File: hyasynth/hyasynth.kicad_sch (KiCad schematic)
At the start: 43 parts, among them J1 Conn_01x04_Male, J2 Conn_01x03_Male, J3 Conn_01x09_Male, J4 Conn_01x05_Male, SW1 Power Switch, SW10 G# Ab, SW11 A, SW12 A# Bb, SW13 B, SW14 C, SW15 Down Octave, SW16 Function, SW17 Up Octave, SW18 Reset, SW2 Low C, SW3 C# Db, SW4 D, SW5 D# Eb, SW6 E, SW7 F, SW8 F# Gb, SW9 G, U1 EFM8LB12F64E-B-QFN32, U2 BH3544F, U3 PAM8302AAD

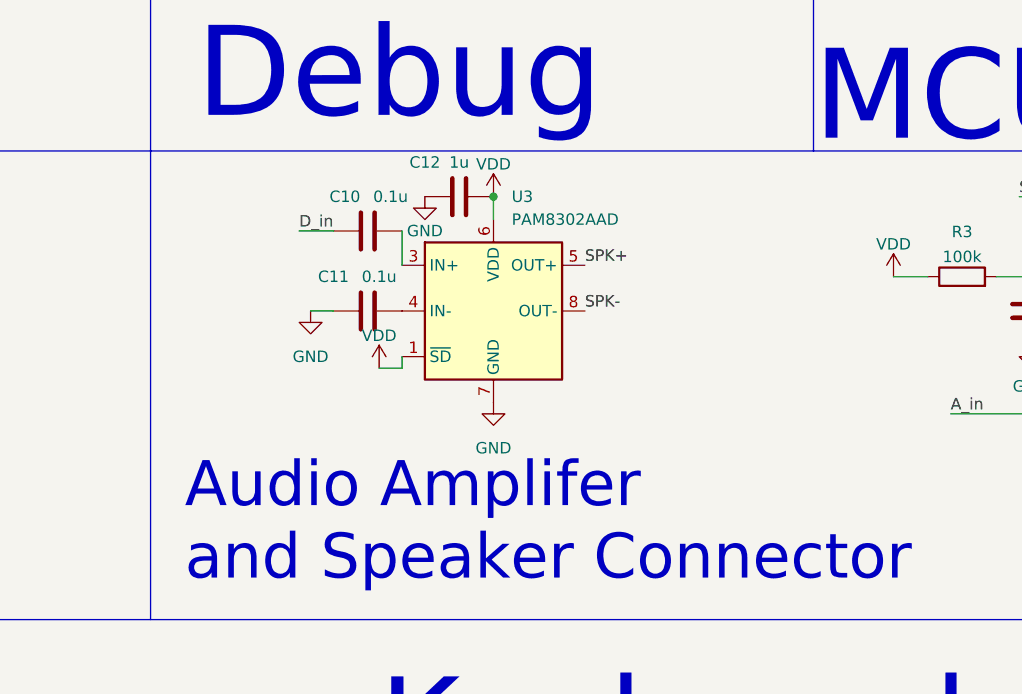
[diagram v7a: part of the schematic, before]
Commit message: started laying out pcb
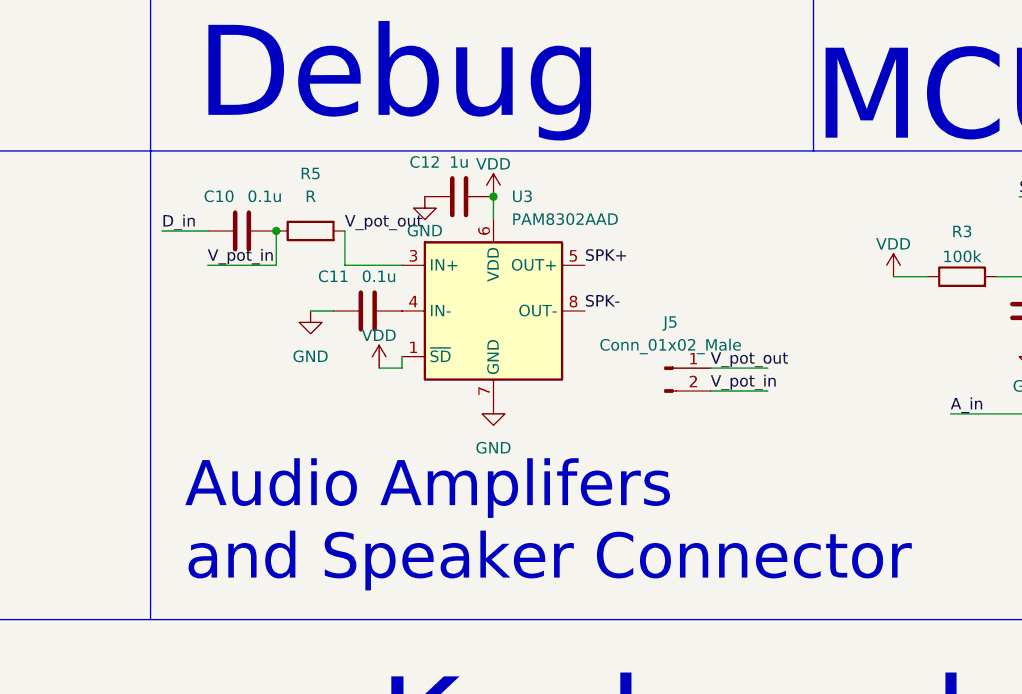
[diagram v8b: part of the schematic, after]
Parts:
- added J5: Conn_01x02_Male, Connector_PinHeader_2.54mm:PinHeader_1x02_P2.54mm_Vertical, symbol Connector:Conn_01x02_Male
- added R5: R, Resistor_SMD:R_0805_2012Metric_Pad1.20x1.40mm_HandSolder, symbol Device:R
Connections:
- net V_pot_in: now reaches C10.2
- net V_pot_in: now also J5.2 (Pin_2), R5.1; no longer U3.3 (IN+)
- new net V_pot_out: J5.1 (Pin_1), R5.2, U3.3 (IN+)
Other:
- note added: "Audio Amplifers and Speaker Connector"
- note removed: "Audio Amplifer and Speaker Connector"
- moved on the sheet: C10
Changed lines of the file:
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@@
   (junction (at 238.76 97.79) (diameter 0) (color 0 0 0 0)
+  )
+  (junction (at 91.44 92.71) (diameter 0) (color 0 0 0 0)
   )
   (junction (at 21.59 175.26) (diameter 0) (color 0 0 0 0)
@@
     (stroke (width 0) (type default) (color 0 0 0 0))
   )
+  (wire (pts (xy 99.06 96.52) (xy 105.41 96.52))
+    (stroke (width 0) (type default) (color 0 0 0 0))
+  )
   (wire (pts (xy 97.79 34.29) (xy 100.33 34.29))
     (stroke (width 0) (type default) (color 0 0 0 0))
@@
     (stroke (width 0) (type default) (color 0 0 0 0))
   )
-  (wire (pts (xy 105.41 92.71) (xy 105.41 96.52))
-    (stroke (width 0) (type default) (color 0 0 0 0))
-  )
-  (wire (pts (xy 93.98 92.71) (xy 97.79 92.71))
+  (wire (pts (xy 78.74 92.71) (xy 83.82 92.71))
     (stroke (width 0) (type default) (color 0 0 0 0))
   )
@@
     (stroke (width 0) (type default) (color 0 0 0 0))
   )
+  (wire (pts (xy 91.44 96.52) (xy 91.44 92.71))
+    (stroke (width 0) (type default) (color 0 0 0 0))
+  )
   (wire (pts (xy 116.84 175.26) (xy 116.84 185.42))
     (stroke (width 0) (type default) (color 0 0 0 0))
   )
+  (wire (pts (xy 139.7 110.49) (xy 146.05 110.49))
+    (stroke (width 0) (type default) (color 0 0 0 0))
+  )
   (wire (pts (xy 187.96 100.33) (xy 187.96 97.79))
     (stroke (width 0) (type default) (color 0 0 0 0))
@@
     (stroke (width 0) (type default) (color 0 0 0 0))
   )
+  (wire (pts (xy 139.7 107.95) (xy 146.05 107.95))
+    (stroke (width 0) (type default) (color 0 0 0 0))
+  )
   (wire (pts (xy 97.79 41.91) (xy 106.68 41.91))
     (stroke (width 0) (type default) (color 0 0 0 0))
@@
     (stroke (width 0) (type default) (color 0 0 0 0))
   )
+  (wire (pts (xy 83.82 96.52) (xy 91.44 96.52))
+    (stroke (width 0) (type default) (color 0 0 0 0))
+  )
   (wire (pts (xy 101.6 175.26) (xy 101.6 167.64))
     (stroke (width 0) (type default) (color 0 0 0 0))
@@
   )
   (wire (pts (xy 21.59 185.42) (xy 38.1 185.42))
+    (stroke (width 0) (type default) (color 0 0 0 0))
+  )
+  (wire (pts (xy 99.06 92.71) (xy 99.06 96.52))
     (stroke (width 0) (type default) (color 0 0 0 0))
   )
@@
     (effects (font (size 10 10)) (justify left bottom))
   )
-  (text "Audio Amplifer \nand Speaker Connector" (at 81.28 132.08 0)
+  (text "Audio Amplifers \nand Speaker Connector" (at 81.28 132.08 0)
     (effects (font (size 5 5)) (justify left bottom))
   )
@@
     (effects (font (size 1.27 1.27)) (justify left bottom))
   )
-  (label "D_in" (at 93.98 92.71 0)
+  (label "D_in" (at 78.74 92.71 0)
     (effects (font (size 1.27 1.27)) (justify left bottom))
   )
@@
   )
   (label "Down" (at 212.09 57.15 0)
+    (effects (font (size 1.27 1.27)) (justify left bottom))
+  )
+  (label "V_pot_out" (at 99.06 92.71 0)
     (effects (font (size 1.27 1.27)) (justify left bottom))
   )
@@
     (effects (font (size 1.27 1.27)) (justify left bottom))
   )
+  (label "V_pot_out" (at 139.7 107.95 0)
+    (effects (font (size 1.27 1.27)) (justify left bottom))
+  )
   (label "DAC" (at 212.09 54.61 0)
     (effects (font (size 1.27 1.27)) (justify left bottom))
@@
     (effects (font (size 1.27 1.27)) (justify left bottom))
   )
+  (label "V_pot_in" (at 83.82 96.52 0)
+    (effects (font (size 1.27 1.27)) (justify left bottom))
+  )
   (label "G" (at 96.52 175.26 0)
     (effects (font (size 1.27 1.27)) (justify left bottom))
   )
   (label "Cntl Common" (at 270.51 158.75 0)
+    (effects (font (size 1.27 1.27)) (justify left bottom))
+  )
+  (label "V_pot_in" (at 139.7 110.49 0)
     (effects (font (size 1.27 1.27)) (justify left bottom))
   )
@@
     )
     (pin "1")
+  )
+  (symbol (lib_id "Device:R") (at 95.25 92.71 90) (unit 1)
+    (in_bom yes) (on_board yes) (fields_autoplaced)
+    (property "Reference" "R5" (id 0) (at 95.25 86.36 90))
+    (property "Value" "R" (id 1) (at 95.25 88.9 90))
+    (property "Footprint" "Resistor_SMD:R_0805_2012Metric_Pad1.20x1.40mm_HandSolder" (id 2) (at 95.25 94.488 90)
+      (effects (font (size 1.27 1.27)) hide)
+    )
+    (property "Datasheet" "~" (id 3) (at 95.25 92.71 0)
+      (effects (font (size 1.27 1.27)) hide)
+    )
+    (pin "1")
+    (pin "2")
   )
   (symbol (lib_id "power:GND") (at 106.68 41.91 0) (unit 1)
@@
     (pin "2")
   )
+  (symbol (lib_id "Connector:Conn_01x02_Male") (at 134.62 107.95 0) (unit 1)
+    (in_bom yes) (on_board yes) (fields_autoplaced)
+    (property "Reference" "J5" (id 0) (at 135.255 102.87 0))
+    (property "Value" "Conn_01x02_Male" (id 1) (at 135.255 105.41 0))
+    (property "Footprint" "Connector_PinHeader_2.54mm:PinHeader_1x02_P2.54mm_Vertical" (id 2) (at 134.62 107.95 0)
+      (effects (font (size 1.27 1.27)) hide)
+    )
+    (property "Datasheet" "~" (id 3) (at 134.62 107.95 0)
+      (effects (font (size 1.27 1.27)) hide)
+    )
+    (pin "1")
+    (pin "2")
+  )
   (symbol (lib_id "Switch:SW_Push") (at 121.92 175.26 0) (unit 1)
     (in_bom yes) (on_board yes) (fields_autoplaced)
@@
     (pin "1")
   )
-  (symbol (lib_id "Device:C") (at 101.6 92.71 90) (unit 1)
+  (symbol (lib_id "Device:C") (at 87.63 92.71 90) (unit 1)
     (in_bom yes) (on_board yes)
-    (property "Reference" "C10" (id 0) (at 99.06 88.9 90))
-    (property "Value" "0.1u" (id 1) (at 104.14 88.9 90))
-    (property "Footprint" "Capacitor_SMD:C_0805_2012Metric_Pad1.18x1.45mm_HandSolder" (id 2) (at 105.41 91.7448 0)
-      (effects (font (size 1.27 1.27)) hide)
-    )
-    (property "Datasheet" "~" (id 3) (at 101.6 92.71 0)
+    (property "Reference" "C10" (id 0) (at 85.09 88.9 90))
+    (property "Value" "0.1u" (id 1) (at 90.17 88.9 90))
+    (property "Footprint" "Capacitor_SMD:C_0805_2012Metric_Pad1.18x1.45mm_HandSolder" (id 2) (at 91.44 91.7448 0)
+      (effects (font (size 1.27 1.27)) hide)
+    )
+    (property "Datasheet" "~" (id 3) (at 87.63 92.71 0)
       (effects (font (size 1.27 1.27)) hide)
     )
@@
       (reference "J4") (unit 1) (value "Conn_01x05_Male") (footprint "Connector_PinHeader_2.54mm:PinHeader_1x05_P2.54mm_Vertical")
     )
+    (path "/6bd9e2e6-f880-4b95-abeb-a7779526b27c"
+      (reference "J5") (unit 1) (value "Conn_01x02_Male") (footprint "Connector_PinHeader_2.54mm:PinHeader_1x02_P2.54mm_Vertical")
+    )
     (path "/e38ef933-cad1-4eee-acc2-e0e397c973b5"
       (reference "R1") (unit 1) (value "10K") (footprint "Resistor_SMD:R_0805_2012Metric_Pad1.20x1.40mm_HandSolder")
@@
       (reference "R4") (unit 1) (value "R") (footprint "Resistor_SMD:R_0805_2012Metric_Pad1.20x1.40mm_HandSolder")
     )
+    (path "/21bba121-79c4-45d0-9265-ddc2938dbd4c"
+      (reference "R5") (unit 1) (value "R") (footprint "Resistor_SMD:R_0805_2012Metric_Pad1.20x1.40mm_HandSolder")
+    )
     (path "/8edc3100-86dd-4549-b6e6-d3e637e4160d"
